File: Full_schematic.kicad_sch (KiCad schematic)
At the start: 215 parts, among them IC1 XC7A100T-1FTG256C, J1 FFC3B11-40-T, J3 Conn_ST_STDC14, SW1 SW_DPST_x2, SW2 SW_DPST_x2, U1 2S7A_0518S1U, U10 MC14511BDG, U11 MAN72A, U12 MC14511BDG, U13 STM32U545VETxQ, U14 MAN72A, U15 MC14511BDG, U16 MAN72A, U17 MC14511BDG, U2 IS66WVE4M16EBLL-70BLI, U3 TPS54294PWP, U4 TPS54325PWPR, U5 SN74ALVC245PWR, U6 IS66WVE4M16EBLL-70BLI, U8 SN74ALVC245PWR, U9 MAN72A, Y1 ASCO, Y2 48MHz

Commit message: C and R footprints
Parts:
- removed C33, C36, C37, C38, C71, C72, C73: 47u, symbol Device:C_Polarized_US
- added C100, C101, C81: 1u, symbol Device:C_Polarized_US
- added C33, C36, C37, C38, C71, C72, C73: 47u, Capacitor_SMD:C_0805_2012Metric, symbol Device:C
- added C81: 100n, Capacitor_SMD:C_0805_2012Metric, symbol Device:C
- added J5: USB_B_Micro, symbol Connector:USB_B_Micro
- C1: footprint (none) -> Capacitor_SMD:C_1210_3225Metric
- C11, C13, C14, C15, C16, C17, C18, C19, C20, C21, C22, C23, C24, C25, C26, C27, C28, C29, C30, C31, C32, C39, C4, C40, C41, C42, C43, C44, C45, C46, C47, C48, C49, C5, C50, C51, C52, C53, C54, C55, C56, C57, C58, C59, C60, C61, C62, C63, C64, C65, C66, C67, C68, C69, C7, C70, C74, C75, C76, C77, C78, C79, C8, C80, C82, C83, C84, C85, C86, C87, C88, C89, C9, C90, C91, C92, C93, C94, C95, C96, C97: footprint (none) -> Capacitor_SMD:C_0805_2012Metric
- C34: footprint (none) -> Capacitor_Tantalum_SMD:CP_EIA-3216-10_Kemet-I
- C35: footprint (none) -> Capacitor_Tantalum_SMD:CP_EIA-2012-15_AVX-P
- R12, R13, R14, R15, R16, R17, R18, R19, R20, R21, R22, R23, R24, R25, R26, R27, R28, R29, R30, R31, R32, R33, R34, R35, R36, R37, R38, R39, R40, R41, R46, R47, R48, R49, R50, R51, R52, R53, R54, R55, R56, R57, R58, R59, R60, R61, R62, R63, R64, R65, R66, R67, R68, R69, R70, R71, R72, R73, R74, R75, R76, R77, R78, R79, R80, R81, R82, R83, R84: footprint (none) -> Resistor_SMD:R_0805_2012Metric
- R42: footprint THB001P_CNK -> joystick:THB001P_CNK
- R43, R44, R45: value 10k -> 1k; footprint (none) -> Resistor_SMD:R_0805_2012Metric
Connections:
- net +1V8: now also C36.1
- net +3.3V: now also R42.3, R42.3', R43.2, R44.2, R45.2; no longer R42.1, R42.1', R42.C, SW1.1 (A), SW2.1 (A)
- net +3V3: now also C33.1, C37.1, C38.1, C71.1, C72.1, C73.1
- net +5V: now also C1.2, C10.1, C10.2, C11.2, C12.1, C12.2, C13.1, C13.2, C14.2, C15.1, C15.2, C16.2, C18.2, C19.2, C2.2, C20.2, C21.2, C22.2, C23.2, C24.2, C25.2, C26.2, C27.1, C28.2, C29.2, C3.1, C30.2, C31.2, C32.2, C34.2, C35.2, C39.2, C4.2, C40.2, C41.2, C42.2, C43.2, C44.2, C45.2, C46.2, C47.2, C48.2, C49.2, C5.2, C51.2, C52.2, C53.2, C55.2, C56.1, C56.2, C57.1, C57.2, C58.2, C59.2, C6.1, C6.2, C60.2, C61.2, C62.2, C63.2, C64.2, C65.2, C66.2, C67.2, C68.2, C69.2, C7.2, C70.2, C74.2, C75.2, C76.2, C77.2, C8.2, C80.2, C82.2, C83.2, C84.2, C85.2, C86.2, C87.2, C88.2, C89.1, C9.2, C90.1, C91.2, C92.2, C93.2, C94.2, C95.2, C96.2, C97.2, C98.2, C99.2, D1.1 (K), IC1.A1 (GND_1), IC1.A11 (GND_2), IC1.B8 (GND_3), IC1.C15 (GND_5), IC1.C5 (GND_4), IC1.D12 (GND_7), IC1.D2 (GND_6), IC1.E9 (GND_8), IC1.F10 (GND_10), IC1.F16 (GND_11), IC1.F6 (GND_9), IC1.F8 (VCCBATT_0), IC1.G13 (GND_14), IC1.G3 (GND_12), IC1.G7 (GNDADC_0), IC1.G9 (GND_13), IC1.H6 (GND_15), IC1.H7 (VREFN_0), IC1.H8 (VP_0), IC1.J11 (GND_17), IC1.J7 (VN_0), IC1.J8 (VREFP_0), IC1.J9 (GND_16), IC1.K14 (GND_20), IC1.K4 (GND_18), IC1.K6 (GND_19), IC1.L1 (GND_21), IC1.L11 (GND_22), IC1.M10 (M1_0), IC1.M11 (M2_0), IC1.M8 (GND_23), IC1.N15 (GND_25), IC1.N5 (GND_24), IC1.P12 (GND_27), IC1.P2 (GND_26), IC1.R9 (GND_28), IC1.T16 (GND_30), IC1.T6 (GND_29), J1.1, J1.13, J1.14, J1.21, J1.22, J1.23, J1.29, J1.3, J1.36, J1.5, J1.6, J1.7, J2.1, J2.11, J2.13, J2.3, J2.5, J2.7, J2.9, J3.5 (GND), J3.7 (GND), J4.10 (CD/GND), J4.11 (EP), J4.6 (VSS), R10.2, R2.2, R4.2, R42.1, R42.1', R42.C, R55.1, SW1.1 (A), SW2.1 (A), U1.2 (-VIN), U1.4 (-VOUT), U10.5 (LE), U10.8 (VSS), U12.5 (LE), U12.8 (VSS), U13.10 (VSS), U13.19 (VSSA), U13.26 (VSS), U13.48 (VSSSMPS), U13.50 (VSS), U13.74 (VSS), U13.99 (VSS), U15.5 (LE), U15.8 (VSS), U17.5 (LE), U17.8 (VSS), U2. (A20), U3.1 (VIN1), U3.13 (PGND2), U3.16 (VIN2), U3.4 (PGND1), U3.8 (GND), U3.EPAD, U4.13 (VIN), U4.14 (VCC), U4.15 (EPAD), U4.5 (GND), U4.7 (EN), U4.8 (PGND1), U4.9 (PGND2), U5.10 (GND), U5.19 (*OE), U6. (A20), U8.10 (GND), U8.19 (*OE), Y1.2 (GND), Y2.2, Y2.4, C100.2, C101.2, C33.2, C36.2, C37.2, C38.2, C71.2, C72.2, C73.2, C81.2, J5.1 (VBUS), J5.5 (GND)
- net PE10: now also C81.1
- net PE11: now also C100.1
- net PE9: now also C101.1
- removed net GND: C1.2, C10.2, C11.2, C12.2, C13.2, C14.2, C15.2, C16.2, C18.2, C19.2, C2.2, C20.2, C21.2, C22.2, C23.2, C24.2, C25.2, C26.2, C27.1, C28.2, C29.2, C3.1, C30.2, C31.2, C32.2, C34.2, C35.2, C39.2, C4.2, C40.2, C41.2, C42.2, C43.2, C44.2, C45.2, C46.2, C47.2, C48.2, C49.2, C5.2, C51.2, C52.2, C53.2, C55.2, C56.2, C57.2, C58.2, C59.2, C6.2, C60.2, C61.2, C62.2, C63.2, C64.2, C65.2, C66.2, C67.2, C68.2, C69.2, C7.2, C70.2, C74.2, C75.2, C76.2, C77.2, C8.2, C80.2, C82.2, C83.2, C84.2, C85.2, C86.2, C87.2, C88.2, C89.1, C9.2, C90.1, C91.2, C92.2, C93.2, C94.2, C95.2, C96.2, C97.2, C98.2, C99.2, D1.1 (K), IC1.A1 (GND_1), IC1.A11 (GND_2), IC1.B8 (GND_3), IC1.C15 (GND_5), IC1.C5 (GND_4), IC1.D12 (GND_7), IC1.D2 (GND_6), IC1.E9 (GND_8), IC1.F10 (GND_10), IC1.F16 (GND_11), IC1.F6 (GND_9), IC1.F8 (VCCBATT_0), IC1.G13 (GND_14), IC1.G3 (GND_12), IC1.G7 (GNDADC_0), IC1.G9 (GND_13), IC1.H6 (GND_15), IC1.H7 (VREFN_0), IC1.H8 (VP_0), IC1.J11 (GND_17), IC1.J7 (VN_0), IC1.J8 (VREFP_0), IC1.J9 (GND_16), IC1.K14 (GND_20), IC1.K4 (GND_18), IC1.K6 (GND_19), IC1.L1 (GND_21), IC1.L11 (GND_22), IC1.M10 (M1_0), IC1.M11 (M2_0), IC1.M8 (GND_23), IC1.N15 (GND_25), IC1.N5 (GND_24), IC1.P12 (GND_27), IC1.P2 (GND_26), IC1.R9 (GND_28), IC1.T16 (GND_30), IC1.T6 (GND_29), J1.1, J1.13, J1.14, J1.21, J1.22, J1.23, J1.29, J1.3, J1.36, J1.5, J1.6, J1.7, J1.S1 (SHIELD), J1.S2 (SHIELD), J2.1, J2.11, J2.13, J2.3, J2.5, J2.7, J2.9, J3.5 (GND), J3.7 (GND), J4.10 (CD/GND), J4.11 (EP), J4.6 (VSS), R10.2, R2.2, R4.2, R42.3, R42.3', R43.2, R44.2, R45.2, R55.1, U1.2 (-VIN), U1.4 (-VOUT), U10.5 (LE), U10.8 (VSS), U12.5 (LE), U12.8 (VSS), U13.10 (VSS), U13.19 (VSSA), U13.26 (VSS), U13.48 (VSSSMPS), U13.50 (VSS), U13.74 (VSS), U13.99 (VSS), U15.5 (LE), U15.8 (VSS), U17.5 (LE), U17.8 (VSS), U2. (A20), U3.13 (PGND2), U3.4 (PGND1), U3.8 (GND), U3.EPAD, U4.15 (EPAD), U4.5 (GND), U4.8 (PGND1), U4.9 (PGND2), U5.10 (GND), U5.19 (*OE), U6. (A20), U8.10 (GND), U8.19 (*OE), Y1.2 (GND), Y2.2, Y2.4
- new net: J1.S1 (SHIELD), J1.S2 (SHIELD)
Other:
- moved on the sheet: R45

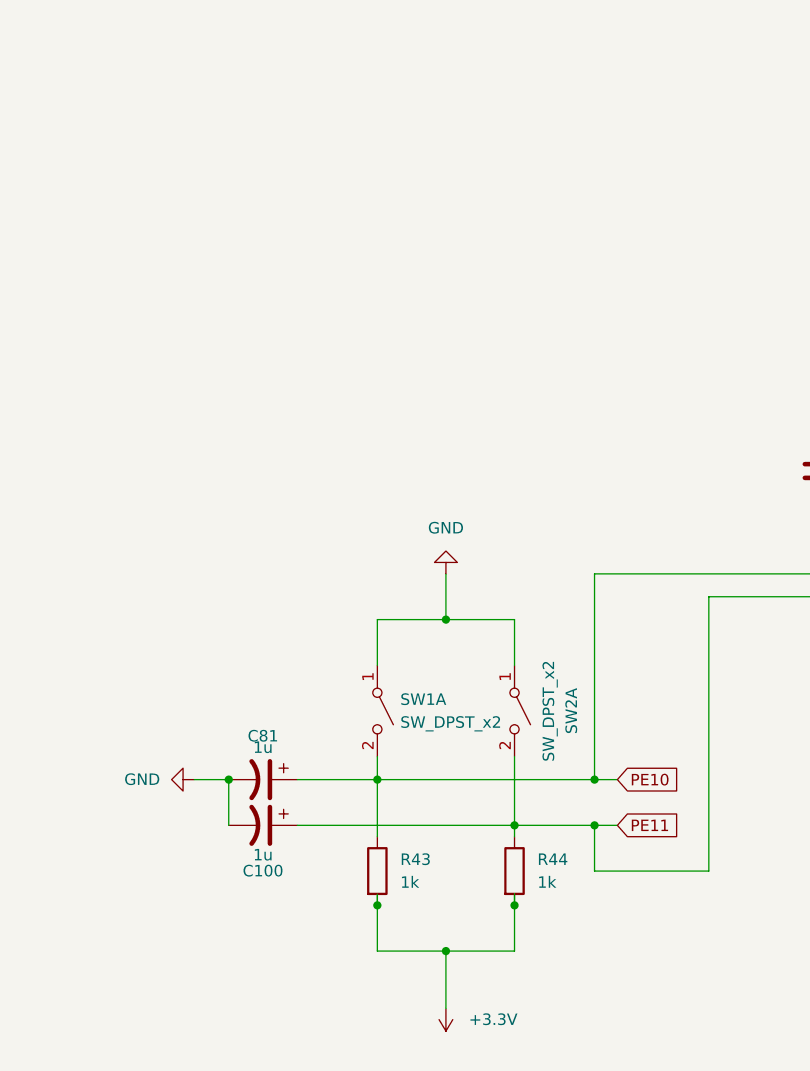
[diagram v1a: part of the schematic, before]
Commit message: updated footprints
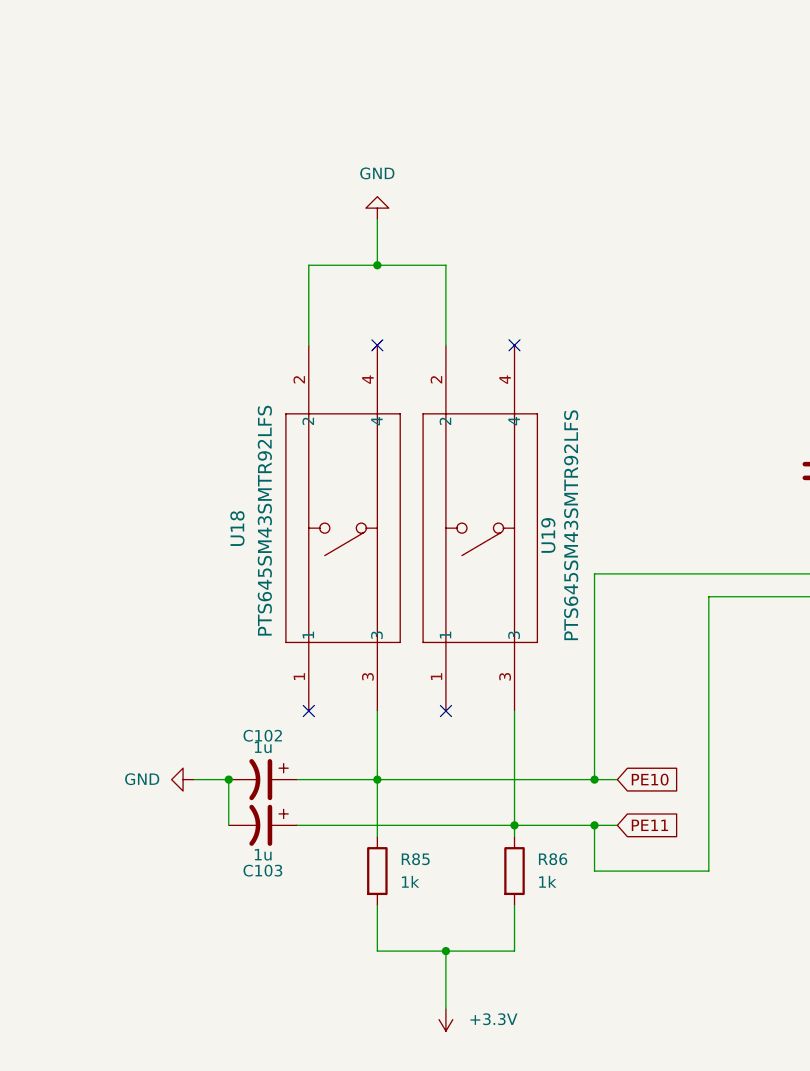
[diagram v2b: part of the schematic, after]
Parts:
- removed C100, C81: 1u, symbol Device:C_Polarized_US
- removed R43, R44: 1k, Resistor_SMD:R_0805_2012Metric, symbol Device:R
- removed SW1, SW2: SW_DPST_x2, symbol Switch:SW_DPST_x2
- added C102, C103: 1u, Capacitor_Tantalum_SMD:CP_EIA-2012-15_AVX-P, symbol Device:C_Polarized_US
- added R85, R86: 1k, Resistor_SMD:R_0805_2012Metric, symbol Device:R
- added U18, U19: PTS645SM43SMTR92LFS, PTS645SM43SMTR92-LFS:SWITCH_43SMTR92LFS, symbol PTS645SM43SMTR92-LFS:PTS645SM43SMTR92LFS
- C101: footprint (none) -> Capacitor_Tantalum_SMD:CP_EIA-2012-15_AVX-P
- C98, C99: footprint (none) -> Capacitor_SMD:C_0805_2012Metric
- IC1: footprint BGA256C100P16X16_1700X1700X155 -> XC7A100T-FTG256:FTG256_AMD
- J1: footprint FFC3B11-40-T:GCT_FFC3B11-40-T -> FFC3BB1-40-T:GCT_FFC3B11-40-T
- J5: footprint (none) -> micro_usbb:CONN_10118192-0002LF_AMP
- L1, L5, L6: footprint (none) -> Inductor_SMD:L_0805_2012Metric
- R5, R6: footprint (none) -> Resistor_SMD:R_0805_2012Metric
- U1: footprint SIP4_2S7A_GAP -> 2S7A_0518S1U:SIP4_2S7A_GAP
- U10, U12, U15, U17: footprint SOIC-16_ONS -> MC14511BDG:SOIC-16_ONS
- U2, U6: footprint (none) -> IS66WVE4M16EBLL-70BLI:TFBGA48_ISI
- U5, U8: footprint PW20 -> SN74ALVC245PWR:PW20
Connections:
- net +3.3V: now also R85.2, R86.2
- net +5V: now also C102.2, C103.2, U18.2, U19.2
- net PE10: now also C102.1, R85.1, U18.3
- net PE11: now also C103.1, R86.1, U19.3
- no-connect marks 121 -> 125

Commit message: commit melding
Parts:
- J2, J3, J4: footprint (none) -> Jumper:Jumper_Harwin_S1621_P10.9mm
- U3: footprint TPS54294PWP:PWP16_2P31X2P46 -> Valve:Valve_EURO
- U4: footprint TPS54325PWPR:PWP14_2P31X2P46 -> Valve:Valve_EURO
- U7: footprint (none) -> 2S7A_0518S1U:SIP4_2S7A_GAP
- Y2: footprint (none) -> Valve:Valve_EURO
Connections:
- net +3.3V: now also C81.1
- net +5V: now also C81.2, J1.S1 (SHIELD), J1.S2 (SHIELD), J5.6 (Shield)
- no-connect marks 125 -> 128
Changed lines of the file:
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@@
 	)
 	(junction
+		(at 615.95 473.71)
+		(diameter 0)
+		(color 0 0 0 0)
+	)
+	(junction
 		(at 43.18 212.09)
 		(diameter 0)
@@
 	)
 	(junction
+		(at 615.95 454.66)
+		(diameter 0)
+		(color 0 0 0 0)
+	)
+	(junction
 		(at 177.8 353.06)
 		(diameter 0)
@@
 	)
 	(no_connect
+		(at 35.56 656.59)
+	)
+	(no_connect
 		(at 220.98 355.6)
 	)
@@
 	)
 	(no_connect
+		(at 35.56 661.67)
+	)
+	(no_connect
 		(at 795.02 554.99)
 	)
@@
 	)
 	(no_connect
+		(at 35.56 659.13)
+	)
+	(no_connect
 		(at 807.72 570.23)
 	)
@@
 	(wire
 		(pts
+			(xy 609.6 468.63) (xy 609.6 473.71)
+		)
+		(stroke
+			(width 0)
+			(type default)
+		)
+	)
+	(wire
+		(pts
 			(xy 731.52 697.23) (xy 731.52 715.01)
 		)
@@
 	(wire
 		(pts
+			(xy 609.6 454.66) (xy 615.95 454.66)
+		)
+		(stroke
+			(width 0)
+			(type default)
+		)
+	)
+	(wire
+		(pts
 			(xy 115.57 171.45) (xy 115.57 168.91)
 		)
@@
 	(wire
 		(pts
+			(xy 609.6 461.01) (xy 609.6 454.66)
+		)
+		(stroke
+			(width 0)
+			(type default)
+		)
+	)
+	(wire
+		(pts
 			(xy 130.81 506.73) (xy 140.97 506.73)
 		)
@@
 	(wire
 		(pts
+			(xy 609.6 473.71) (xy 615.95 473.71)
+		)
+		(stroke
+			(width 0)
+			(type default)
+		)
+	)
+	(wire
+		(pts
 			(xy 304.8 129.54) (xy 313.69 129.54)
 		)
@@
 	(wire
 		(pts
+			(xy 25.4 671.83) (xy 25.4 666.75)
+		)
+		(stroke
+			(width 0)
+			(type default)
+		)
+	)
+	(wire
+		(pts
 			(xy 706.12 478.79) (xy 706.12 481.33)
 		)
@@
 	)
 	(symbol
+		(lib_id "power:GND")
+		(at 25.4 671.83 0)
+		(unit 1)
+		(exclude_from_sim no)
+		(in_bom yes)
+		(on_board yes)
+		(dnp no)
+		(fields_autoplaced yes)
+		(property "Reference" "#PWR0116"
+			(at 25.4 678.18 0)
+			(effects
+				(font
+					(size 1.27 1.27)
+				)
+				(hide yes)
+			)
+		)
+		(property "Value" "GND"
+			(at 25.4 676.91 0)
+			(effects
+				(font
+					(size 1.27 1.27)
+				)
+			)
+		)
+		(property "Footprint" ""
+			(at 25.4 671.83 0)
+			(effects
+				(font
+					(size 1.27 1.27)
+				)
+				(hide yes)
+			)
+		)
+		(property "Datasheet" ""
+			(at 25.4 671.83 0)
+			(effects
+				(font
+					(size 1.27 1.27)
+				)
+				(hide yes)
+			)
+		)
+		(property "Description" "Power symbol creates a global label with name \"GND\" , ground"
+			(at 25.4 671.83 0)
+			(effects
+				(font
+					(size 1.27 1.27)
+				)
+				(hide yes)
+			)
+		)
+		(pin "1"
+		)
+		(instances
+			(project "Full_schematic"
+				(path "/f31f37d2-6847-4047-ac5f-32db6fac168c"
+					(reference "#PWR0116")
+					(unit 1)
+				)
+			)
+		)
+	)
+	(symbol
 		(lib_id "Device:C")
 		(at 378.46 557.53 0)
@@
 			)
 		)
-		(property "Footprint" "TPS54294PWP:PWP16_2P31X2P46"
+		(property "Footprint" "Valve:Valve_EURO"
 			(at 120.65 764.54 0)
 			(effects
@@
 			)
 		)
-		(property "Footprint" ""
+		(property "Footprint" "Jumper:Jumper_Harwin_S1621_P10.9mm"
 			(at 919.48 610.87 0)
 			(effects
@@
 			)
 		)
-		(property "Footprint" ""
+		(property "Footprint" "Valve:Valve_EURO"
 			(at 604.52 516.89 0)
 			(effects
@@
 	)
 	(symbol
-		(lib_id "power:PWR_FLAG")
-		(at 49.53 675.64 0)
-		(unit 1)
-		(exclude_from_sim no)
-		(in_bom yes)
-		(on_board yes)
-		(dnp no)
-		(property "Reference" "#FLG01"
-			(at 49.53 673.735 0)
-			(effects
-				(font
-					(size 1.27 1.27)
-				)
-				(hide yes)
-			)
-		)
-		(property "Value" "PWR_FLAG"
-			(at 49.53 670.56 0)
-			(effects
-				(font
-					(size 1.27 1.27)
-				)
-			)
-		)
-		(property "Footprint" ""
-			(at 49.53 675.64 0)
-			(effects
-				(font
-					(size 1.27 1.27)
-				)
-				(hide yes)
-			)
-		)
-		(property "Datasheet" "~"
-			(at 49.53 675.64 0)
-			(effects
-				(font
-					(size 1.27 1.27)
-				)
-				(hide yes)
-			)
-		)
-		(property "Description" "4.5V - 18V"
-			(at 49.53 675.64 0)
-			(effects
-				(font
-					(size 1.27 1.27)
-				)
-			)
-		)
-		(pin "1"
-		)
-		(instances
-			(project "Full_schematic"
-				(path "/f31f37d2-6847-4047-ac5f-32db6fac168c"
-					(reference "#FLG01")
-					(unit 1)
-				)
-			)
-		)
-	)
-	(symbol
 		(lib_id "power:GND")
 		(at 304.8 66.04 90)
@@
 	)
 	(symbol
-		(lib_id "power:PWR_FLAG")
-		(at 35.56 203.2 90)
-		(unit 1)
-		(exclude_from_sim no)
-		(in_bom yes)
-		(on_board yes)
-		(dnp no)
-		(fields_autoplaced yes)
-		(property "Reference" "#FLG08"
-			(at 33.655 203.2 0)
-			(effects
-				(font
-					(size 1.27 1.27)
-				)
-				(hide yes)
-			)
-		)
-		(property "Value" "PWR_FLAG"
-			(at 31.75 203.1999 90)
-			(effects
-				(font
-					(size 1.27 1.27)
-				)
-				(justify left)
-			)
-		)
-		(property "Footprint" ""
-			(at 35.56 203.2 0)
-			(effects
-				(font
-					(size 1.27 1.27)
-				)
-				(hide yes)
-			)
-		)
-		(property "Datasheet" "~"
-			(at 35.56 203.2 0)
-			(effects
-				(font
-					(size 1.27 1.27)
-				)
-				(hide yes)
-			)
-		)
-		(property "Description" "Special symbol for telling ERC where power comes from"
-			(at 35.56 203.2 0)
-			(effects
-				(font
-					(size 1.27 1.27)
-				)
-				(hide yes)
-			)
-		)
-		(pin "1"
-		)
-		(instances
-			(project "Full_schematic"
-				(path "/f31f37d2-6847-4047-ac5f-32db6fac168c"
-					(reference "#FLG08")
-					(unit 1)
-				)
-			)
-		)
-	)
-	(symbol
 		(lib_id "power:+3V3")
 		(at 220.98 365.76 90)
@@
 	)
 	(symbol
+		(lib_id "power:GND")
+		(at 39.37 21.59 90)
+		(unit 1)
+		(exclude_from_sim no)
+		(in_bom yes)
+		(on_board yes)
+		(dnp no)
+		(fields_autoplaced yes)
+		(property "Reference" "#PWR0115"
+			(at 45.72 21.59 0)
+			(effects
+				(font
+					(size 1.27 1.27)
+				)
+				(hide yes)
+			)
+		)
+		(property "Value" "GND"
+			(at 43.18 21.5901 90)
+			(effects
+				(font
+					(size 1.27 1.27)
+				)
+				(justify right)
+			)
+		)
+		(property "Footprint" ""
+			(at 39.37 21.59 0)
+			(effects
+				(font
+					(size 1.27 1.27)
+				)
+				(hide yes)
+			)
+		)
+		(property "Datasheet" ""
+			(at 39.37 21.59 0)
+			(effects
+				(font
+					(size 1.27 1.27)
+				)
+				(hide yes)
+			)
+		)
+		(property "Description" "Power symbol creates a global label with name \"GND\" , ground"
+			(at 39.37 21.59 0)
+			(effects
+				(font
+					(size 1.27 1.27)
+				)
+				(hide yes)
+			)
+		)
+		(pin "1"
+		)
+		(instances
+			(project "Full_schematic"
+				(path "/f31f37d2-6847-4047-ac5f-32db6fac168c"
+					(reference "#PWR0115")
+					(unit 1)
+				)
+			)
+		)
+	)
+	(symbol
 		(lib_id "Device:C_Polarized_US")
 		(at 77.47 684.53 0)
@@
 			)
 		)
-		(property "Footprint" "TPS54325PWPR:PWP14_2P31X2P46"
+		(property "Footprint" "Valve:Valve_EURO"
 			(at 162.56 697.23 0)
 			(effects
@@
 			)
 		)
-		(property "Footprint" ""
+		(property "Footprint" "2S7A_0518S1U:SIP4_2S7A_GAP"
 			(at 447.04 101.6 0)
 			(effects
@@
 			)
 		)
-		(property "Footprint" ""
+		(property "Footprint" "Jumper:Jumper_Harwin_S1621_P10.9mm"
 			(at 789.94 567.69 0)
 			(effects
@@
 			)
 		)
-		(property "Footprint" ""
+		(property "Footprint" "Jumper:Jumper_Harwin_S1621_P10.9mm"
 			(at 420.37 194.31 0)
 			(effects

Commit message: Fixed schematic comments
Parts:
- removed C81: 100n, Capacitor_SMD:C_0805_2012Metric, symbol Device:C
- removed L5: FerriteBead, Inductor_SMD:L_0805_2012Metric, symbol Device:FerriteBead
- removed R11: 1, Resistor_SMD:R_0805_2012Metric, symbol Device:R
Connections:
- net +3.3VA is gone; now on net +3.3V: C94.1, C95.1, U13.21 (VDDA)
- net +1V0: now also IC1.K9 (VCCINT_6)
- net +3V3: now also IC1.B3 (VCCO_35_2), IC1.D7 (VCCO_35_3), IC1.F1 (VCCO_35_5), IC1.M3 (VCCO_34_1), IC1.M9 (M0_0), IC1.R4 (VCCO_34_2), IC1.T1 (VCCO_34_3)
- no-connect marks 128 -> 120
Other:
- moved on the sheet: C18

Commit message: commit melding
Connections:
- net L12: now also IC1.T12 (IO_L15N_T2_DQS_DOUT_CSO_B_14); no longer IC1.L12 (IO_L6P_T0_FCS_B_14)
- net T12: no longer names the net of U7.1 (CS#)
- net T12: now also IC1.L12 (IO_L6P_T0_FCS_B_14); no longer IC1.T12 (IO_L15N_T2_DQS_DOUT_CSO_B_14)
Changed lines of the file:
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@@
 	(wire
 		(pts
-			(xy 482.6 110.49) (xy 482.6 358.14)
-		)
-		(stroke
-			(width 0)
-			(type default)
-		)
-	)
-	(wire
-		(pts
 			(xy 666.75 588.01) (xy 666.75 675.64)
 		)
@@
 	(wire
 		(pts
+			(xy 474.98 154.94) (xy 474.98 110.49)
+		)
+		(stroke
+			(width 0)
+			(type default)
+		)
+	)
+	(wire
+		(pts
 			(xy 336.55 238.76) (xy 388.62 238.76)
 		)
@@
 	(wire
 		(pts
-			(xy 482.6 110.49) (xy 452.12 110.49)
-		)
-		(stroke
-			(width 0)
-			(type default)
-		)
-	)
-	(wire
-		(pts
 			(xy 450.85 320.04) (xy 450.85 382.27)
 		)
@@
 	(wire
 		(pts
-			(xy 304.8 358.14) (xy 482.6 358.14)
+			(xy 304.8 358.14) (xy 331.47 358.14)
 		)
 		(stroke
@@
 	(wire
 		(pts
-			(xy 331.47 154.94) (xy 331.47 252.73)
-		)
-		(stroke
-			(width 0)
-			(type default)
-		)
-	)
-	(wire
-		(pts
 			(xy 134.62 666.75) (xy 99.06 666.75)
 		)
@@
 	(wire
 		(pts
+			(xy 474.98 110.49) (xy 452.12 110.49)
+		)
+		(stroke
+			(width 0)
+			(type default)
+		)
+	)
+	(wire
+		(pts
 			(xy 120.65 749.3) (xy 191.77 749.3)
 		)
@@
 	(wire
 		(pts
-			(xy 304.8 154.94) (xy 331.47 154.94)
+			(xy 304.8 154.94) (xy 474.98 154.94)
 		)
 		(stroke
@@
 	(wire
 		(pts
+			(xy 331.47 358.14) (xy 331.47 252.73)
+		)
+		(stroke
+			(width 0)
+			(type default)
+		)
+	)
+	(wire
+		(pts
 			(xy 347.98 245.11) (xy 347.98 241.3)
 		)
@@
 				(hide yes)
 			)
-		)
-	)
-	(global_label "T12"
-		(shape input)
-		(at 482.6 358.14 0)
-		(fields_autoplaced yes)
-		(effects
-			(font
-				(size 1.27 1.27)
-			)
-			(justify left)
-		)
-		(property "Intersheetrefs" "${INTERSHEET_REFS}"
-			(at 488.9718 358.14 0)
-			(effects
-				(font
-					(size 1.27 1.27)
-				)
-				(justify left)
-				(hide yes)
-			)

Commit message: --amend
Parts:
- C38, C73: value 47u -> 4.7u
- U3: footprint Valve:Valve_EURO -> (none)
- U4: footprint Valve:Valve_EURO -> TPS54325PWPR:PWP14_2P31X2P46
- U7: value ~ -> S25FL127S; footprint 2S7A_0518S1U:SIP4_2S7A_GAP -> footprints:SO3016_INF
- Y1: footprint Oscillator:Oscillator_SMD_Abracon_ASCO-4Pin_1.6x1.2mm -> WW100:XTAL_ASV-100.000MHZ-EC-T
- Y2: footprint Valve:Valve_EURO -> WW100:XTAL_ASV-100.000MHZ-EC-T
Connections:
- net +5V: no longer C1.2, C10.2, C101.2, C102.2, C103.2, C11.2, C12.2, C13.2, C14.2, C15.2, C16.2, C18.2, C19.2, C2.2, C20.2, C21.2, C22.2, C23.2, C24.2, C25.2, C26.2, C27.1, C28.2, C29.2, C3.1, C30.2, C31.2, C32.2, C33.2, C34.2, C35.2, C36.2, C37.2, C38.2, C39.2, C4.2, C40.2, C41.2, C42.2, C43.2, C44.2, C45.2, C46.2, C47.2, C48.2, C49.2, C5.2, C51.2, C52.2, C53.2, C55.2, C56.2, C57.2, C58.2, C59.2, C6.2, C60.2, C61.2, C62.2, C63.2, C64.2, C65.2, C66.2, C67.2, C68.2, C69.2, C7.2, C70.2, C71.2, C72.2, C73.2, C74.2, C75.2, C76.2, C77.2, C8.2, C80.2, C82.2, C83.2, C84.2, C85.2, C86.2, C87.2, C88.2, C89.1, C9.2, C90.1, C91.2, C92.2, C93.2, C94.2, C95.2, C96.2, C97.2, C98.2, C99.2, D1.1 (K), IC1.A1 (GND_1), IC1.A11 (GND_2), IC1.B8 (GND_3), IC1.C15 (GND_5), IC1.C5 (GND_4), IC1.D12 (GND_7), IC1.D2 (GND_6), IC1.E9 (GND_8), IC1.F10 (GND_10), IC1.F16 (GND_11), IC1.F6 (GND_9), IC1.F8 (VCCBATT_0), IC1.G13 (GND_14), IC1.G3 (GND_12), IC1.G7 (GNDADC_0), IC1.G9 (GND_13), IC1.H6 (GND_15), IC1.H7 (VREFN_0), IC1.H8 (VP_0), IC1.J11 (GND_17), IC1.J7 (VN_0), IC1.J8 (VREFP_0), IC1.J9 (GND_16), IC1.K14 (GND_20), IC1.K4 (GND_18), IC1.K6 (GND_19), IC1.L1 (GND_21), IC1.L11 (GND_22), IC1.M10 (M1_0), IC1.M11 (M2_0), IC1.M8 (GND_23), IC1.N15 (GND_25), IC1.N5 (GND_24), IC1.P12 (GND_27), IC1.P2 (GND_26), IC1.R9 (GND_28), IC1.T16 (GND_30), IC1.T6 (GND_29), J1.1, J1.13, J1.14, J1.21, J1.22, J1.23, J1.29, J1.3, J1.36, J1.5, J1.6, J1.7, J1.S1 (SHIELD), J1.S2 (SHIELD), J2.1, J2.11, J2.13, J2.3, J2.5, J2.7, J2.9, J3.5 (GND), J3.7 (GND), J4.10 (CD/GND), J4.11 (EP), J4.6 (VSS), J5.5 (GND), J5.6 (Shield), R10.2, R2.2, R4.2, R42.1, R42.1', R42.C, R55.1, U1.2 (-VIN), U1.4 (-VOUT), U10.5 (LE), U10.8 (VSS), U12.5 (LE), U12.8 (VSS), U13.10 (VSS), U13.19 (VSSA), U13.26 (VSS), U13.48 (VSSSMPS), U13.50 (VSS), U13.74 (VSS), U13.99 (VSS), U15.5 (LE), U15.8 (VSS), U17.5 (LE), U17.8 (VSS), U18.2, U19.2, U2. (A20), U3.13 (PGND2), U3.4 (PGND1), U3.8 (GND), U3.EPAD, U4.15 (EPAD), U4.5 (GND), U4.8 (PGND1), U4.9 (PGND2), U5.10 (GND), U5.19 (*OE), U6. (A20), U8.10 (GND), U8.19 (*OE), Y1.2 (GND), Y2.2, Y2.4
- new net GND: C1.2, C10.2, C101.2, C102.2, C103.2, C11.2, C12.2, C13.2, C14.2, C15.2, C16.2, C18.2, C19.2, C2.2, C20.2, C21.2, C22.2, C23.2, C24.2, C25.2, C26.2, C27.1, C28.2, C29.2, C3.1, C30.2, C31.2, C32.2, C33.2, C34.2, C35.2, C36.2, C37.2, C38.2, C39.2, C4.2, C40.2, C41.2, C42.2, C43.2, C44.2, C45.2, C46.2, C47.2, C48.2, C49.2, C5.2, C51.2, C52.2, C53.2, C55.2, C56.2, C57.2, C58.2, C59.2, C6.2, C60.2, C61.2, C62.2, C63.2, C64.2, C65.2, C66.2, C67.2, C68.2, C69.2, C7.2, C70.2, C71.2, C72.2, C73.2, C74.2, C75.2, C76.2, C77.2, C8.2, C80.2, C82.2, C83.2, C84.2, C85.2, C86.2, C87.2, C88.2, C89.1, C9.2, C90.1, C91.2, C92.2, C93.2, C94.2, C95.2, C96.2, C97.2, C98.2, C99.2, D1.1 (K), IC1.A1 (GND_1), IC1.A11 (GND_2), IC1.B8 (GND_3), IC1.C15 (GND_5), IC1.C5 (GND_4), IC1.D12 (GND_7), IC1.D2 (GND_6), IC1.E9 (GND_8), IC1.F10 (GND_10), IC1.F16 (GND_11), IC1.F6 (GND_9), IC1.F8 (VCCBATT_0), IC1.G13 (GND_14), IC1.G3 (GND_12), IC1.G7 (GNDADC_0), IC1.G9 (GND_13), IC1.H6 (GND_15), IC1.H7 (VREFN_0), IC1.H8 (VP_0), IC1.J11 (GND_17), IC1.J7 (VN_0), IC1.J8 (VREFP_0), IC1.J9 (GND_16), IC1.K14 (GND_20), IC1.K4 (GND_18), IC1.K6 (GND_19), IC1.L1 (GND_21), IC1.L11 (GND_22), IC1.M10 (M1_0), IC1.M11 (M2_0), IC1.M8 (GND_23), IC1.N15 (GND_25), IC1.N5 (GND_24), IC1.P12 (GND_27), IC1.P2 (GND_26), IC1.R9 (GND_28), IC1.T16 (GND_30), IC1.T6 (GND_29), J1.1, J1.13, J1.14, J1.21, J1.22, J1.23, J1.29, J1.3, J1.36, J1.5, J1.6, J1.7, J1.S1 (SHIELD), J1.S2 (SHIELD), J2.1, J2.11, J2.13, J2.3, J2.5, J2.7, J2.9, J3.5 (GND), J3.7 (GND), J4.10 (CD/GND), J4.11 (EP), J4.6 (VSS), J5.5 (GND), J5.6 (Shield), R10.2, R2.2, R4.2, R42.1, R42.1', R42.C, R55.1, U1.2 (-VIN), U1.4 (-VOUT), U10.5 (LE), U10.8 (VSS), U12.5 (LE), U12.8 (VSS), U13.10 (VSS), U13.19 (VSSA), U13.26 (VSS), U13.48 (VSSSMPS), U13.50 (VSS), U13.74 (VSS), U13.99 (VSS), U15.5 (LE), U15.8 (VSS), U17.5 (LE), U17.8 (VSS), U18.2, U19.2, U2. (A20), U3.13 (PGND2), U3.4 (PGND1), U3.8 (GND), U3.EPAD, U4.15 (EPAD), U4.5 (GND), U4.8 (PGND1), U4.9 (PGND2), U5.10 (GND), U5.19 (*OE), U6. (A20), U8.10 (GND), U8.19 (*OE), Y1.2 (GND), Y2.2, Y2.4
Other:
- note added: "S25FL128SAGMFI000"
- note removed: "S25FL127S"
- note removed: "U1"

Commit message: commit melding
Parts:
- J1: footprint FFC3BB1-40-T:GCT_FFC3B11-40-T -> KiCad:FH12A40S05SH55
- U3: footprint (none) -> KiCad:FH12A40S05SH55
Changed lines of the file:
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@@
 			)
 		)
-		(property "Footprint" ""
+		(property "Footprint" "KiCad:FH12A40S05SH55"
 			(at 120.65 764.54 0)
 			(effects
@@
 			)
 		)
-		(property "Footprint" "FFC3BB1-40-T:GCT_FFC3B11-40-T"
+		(property "Footprint" "KiCad:FH12A40S05SH55"
 			(at 29.21 74.93 0)
 			(effects
